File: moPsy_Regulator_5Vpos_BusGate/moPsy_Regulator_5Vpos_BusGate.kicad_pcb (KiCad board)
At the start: 2 copper layers, 64 x 40 mm, 24 parts, among them J1 Conn_01x01_Male, J11 Conn_01x01_Male, J13 Conn_01x01_Male, J15 Conn_01x01_Male, J18 Conn_01x01_Male, J19 Conn_01x01_Male, J2 Conn_01x01_Male, J3 Conn_01x01_Male, J5 Conn_01x01_Male, J7 Conn_01x01_Male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

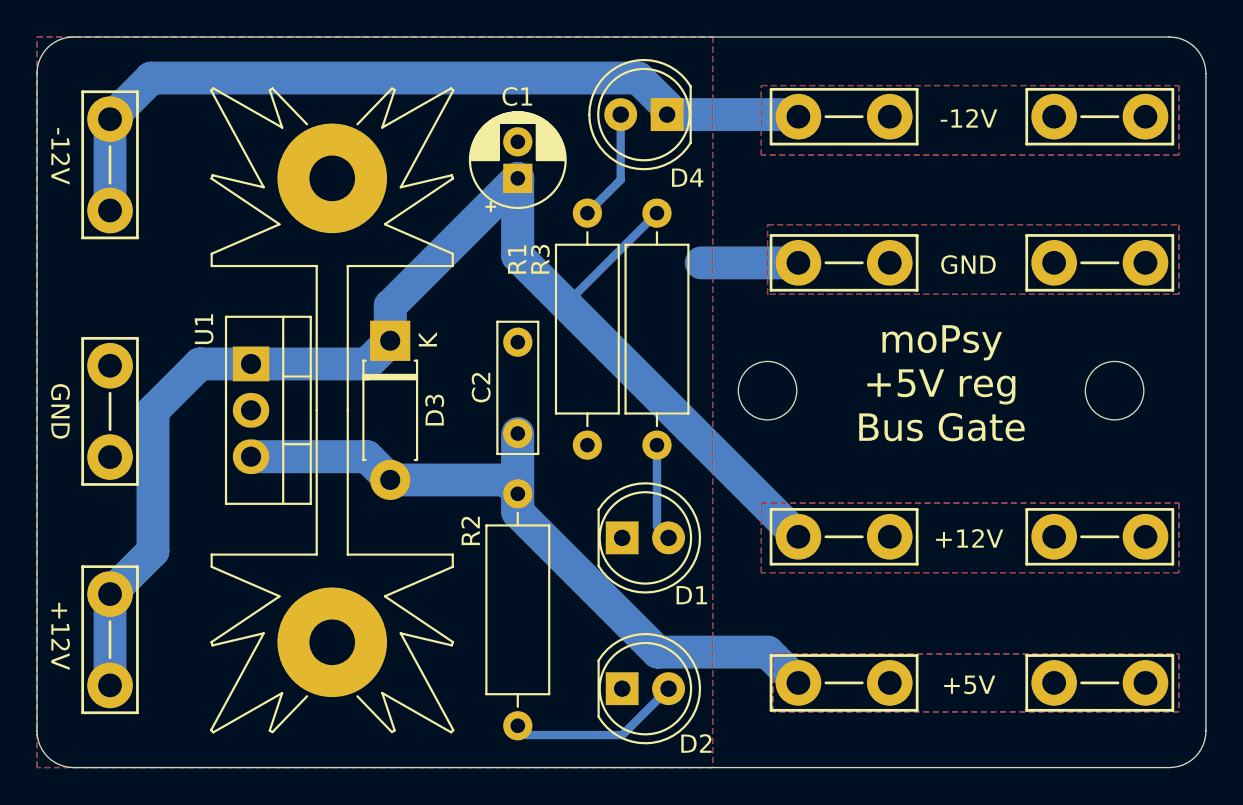
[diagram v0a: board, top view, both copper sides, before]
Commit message: Add OSHW logo to 5Vpos BusGate PCB
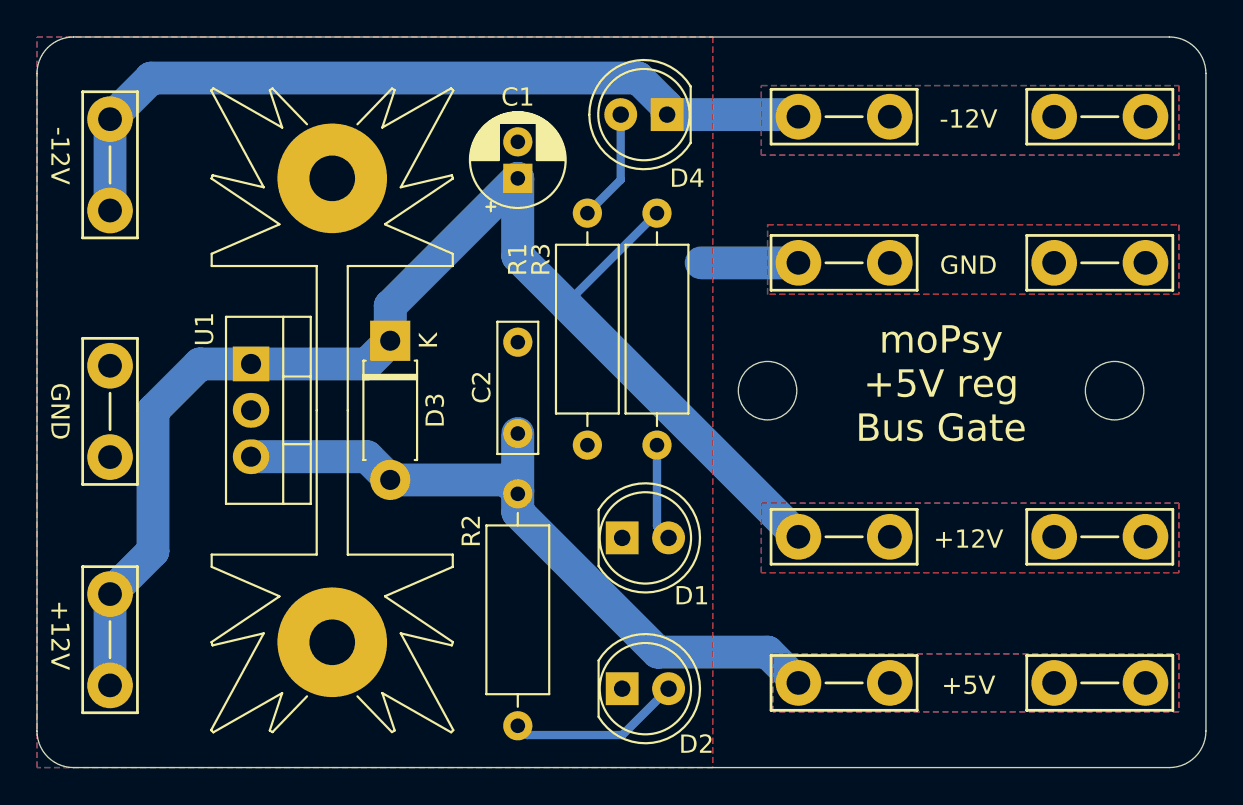
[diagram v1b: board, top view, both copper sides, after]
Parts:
- added REF**: OSHW-Logo2_7.3x6mm_SilkScreen, Symbol:OSHW-Logo2_7.3x6mm_SilkScreen, B.Cu at (170.8, 83.2)
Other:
- net class Default removed
- net class PWR removed
